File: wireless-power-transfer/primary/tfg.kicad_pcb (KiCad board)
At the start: 2 copper layers, 160 x 100 mm, 35 parts, among them J1 CONN_01X06, J2 Screw_Terminal_1x02, J3 BARREL_JACK, Q1 IRLB8721PBF, Q2 IRLB8721PBF, Q3 IRLB8721PBF, Q4 IRLB8721PBF, U1 PIC18F45K20-I/PT, U2 IR2110, U3 IR2110, U4 R-78E15, U5 R-78E3.3, U6 XBEE_Wi-Fi

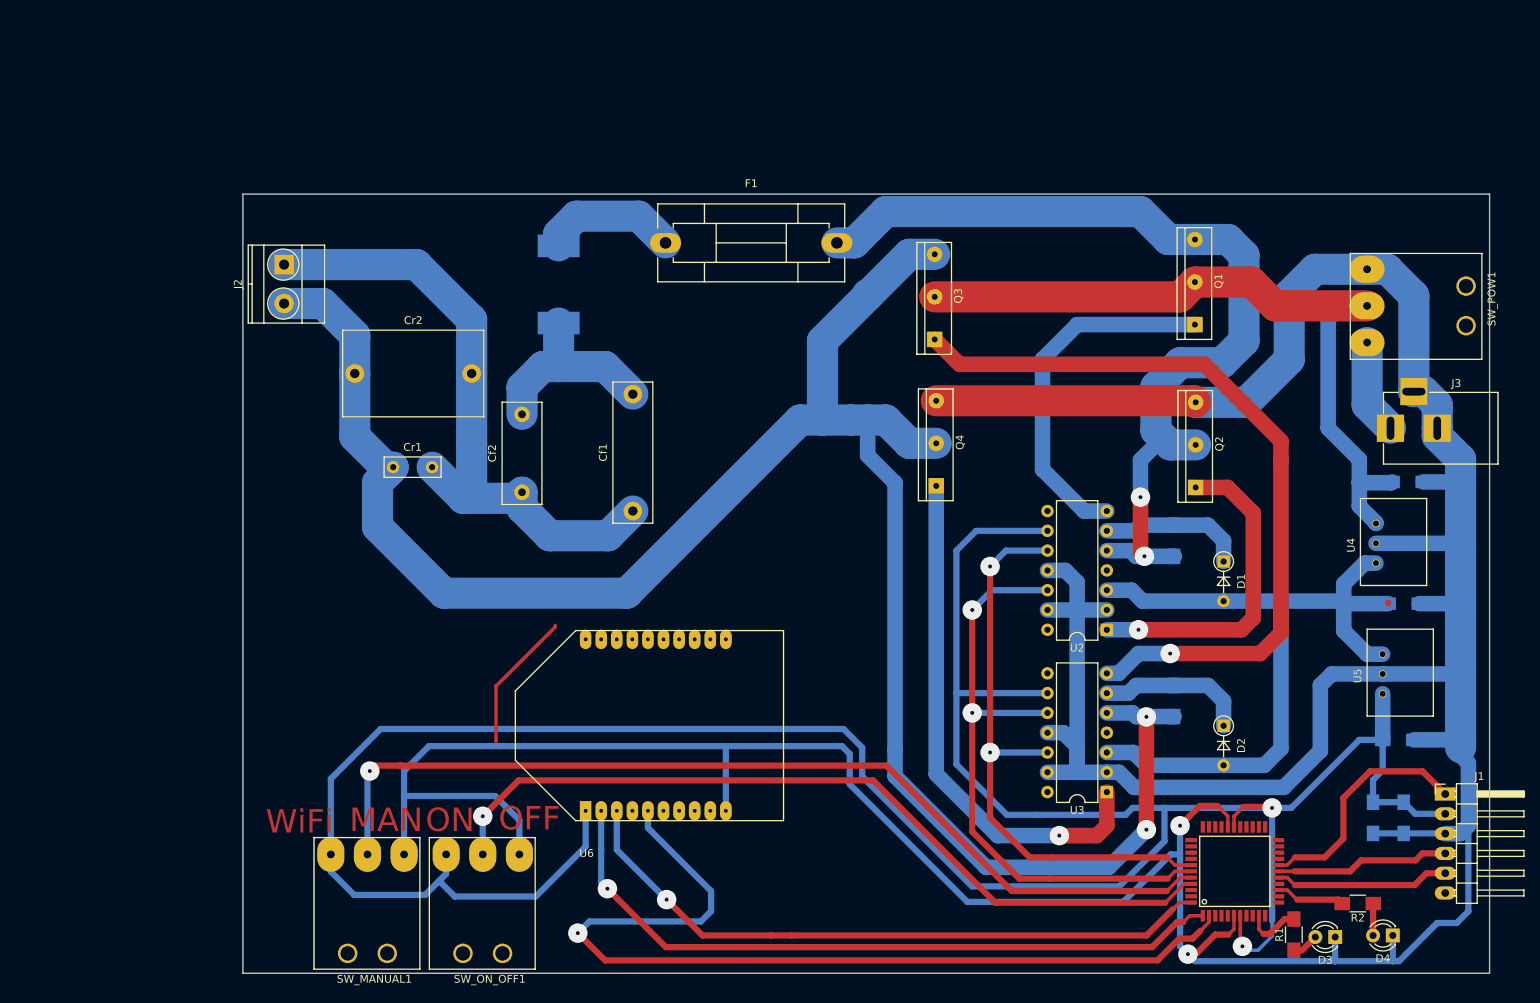
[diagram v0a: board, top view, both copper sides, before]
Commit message: Modified traces for giving some margin to the edges of the board.
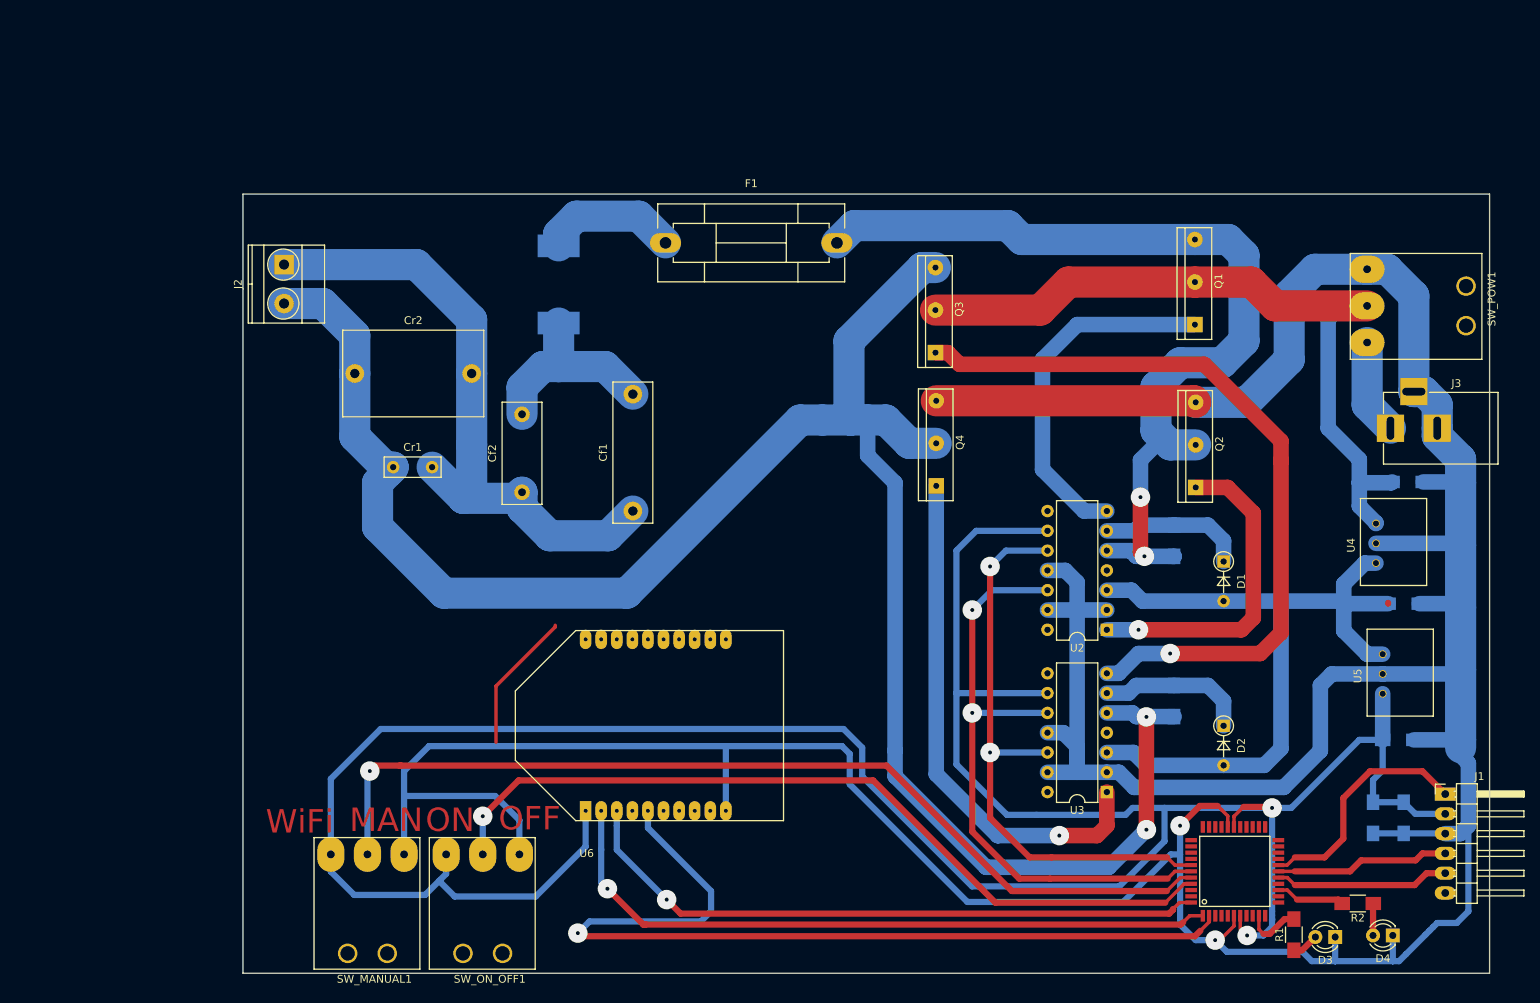
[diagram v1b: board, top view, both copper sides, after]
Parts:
- moved Q3 1.70 mm to (174.6, 67.3)
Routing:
- net Net-(C1-Pad2): track 550.2 -> 543.9 mm
- net Net-(Cboot2-Pad2): track 264.3 -> 260.2 mm
- net /+3.3V: track 355.0 -> 351.7 mm
- net Net-(U1-Pad2): track 119.8 -> 117.3 mm
- net Net-(U1-Pad44): track 85.0 -> 82.8 mm
- net Net-(U1-Pad1): track 91.5 -> 89.4 mm
- net Net-(Cboot1-Pad2): track 122.2 -> 120.7 mm
- net Net-(Q3-Pad1): track 99.2 -> 98.4 mm
- net Net-(C5-Pad1): track 96.3 -> 96.9 mm

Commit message: PCB modified extracting the filter and the tank to another PCB.
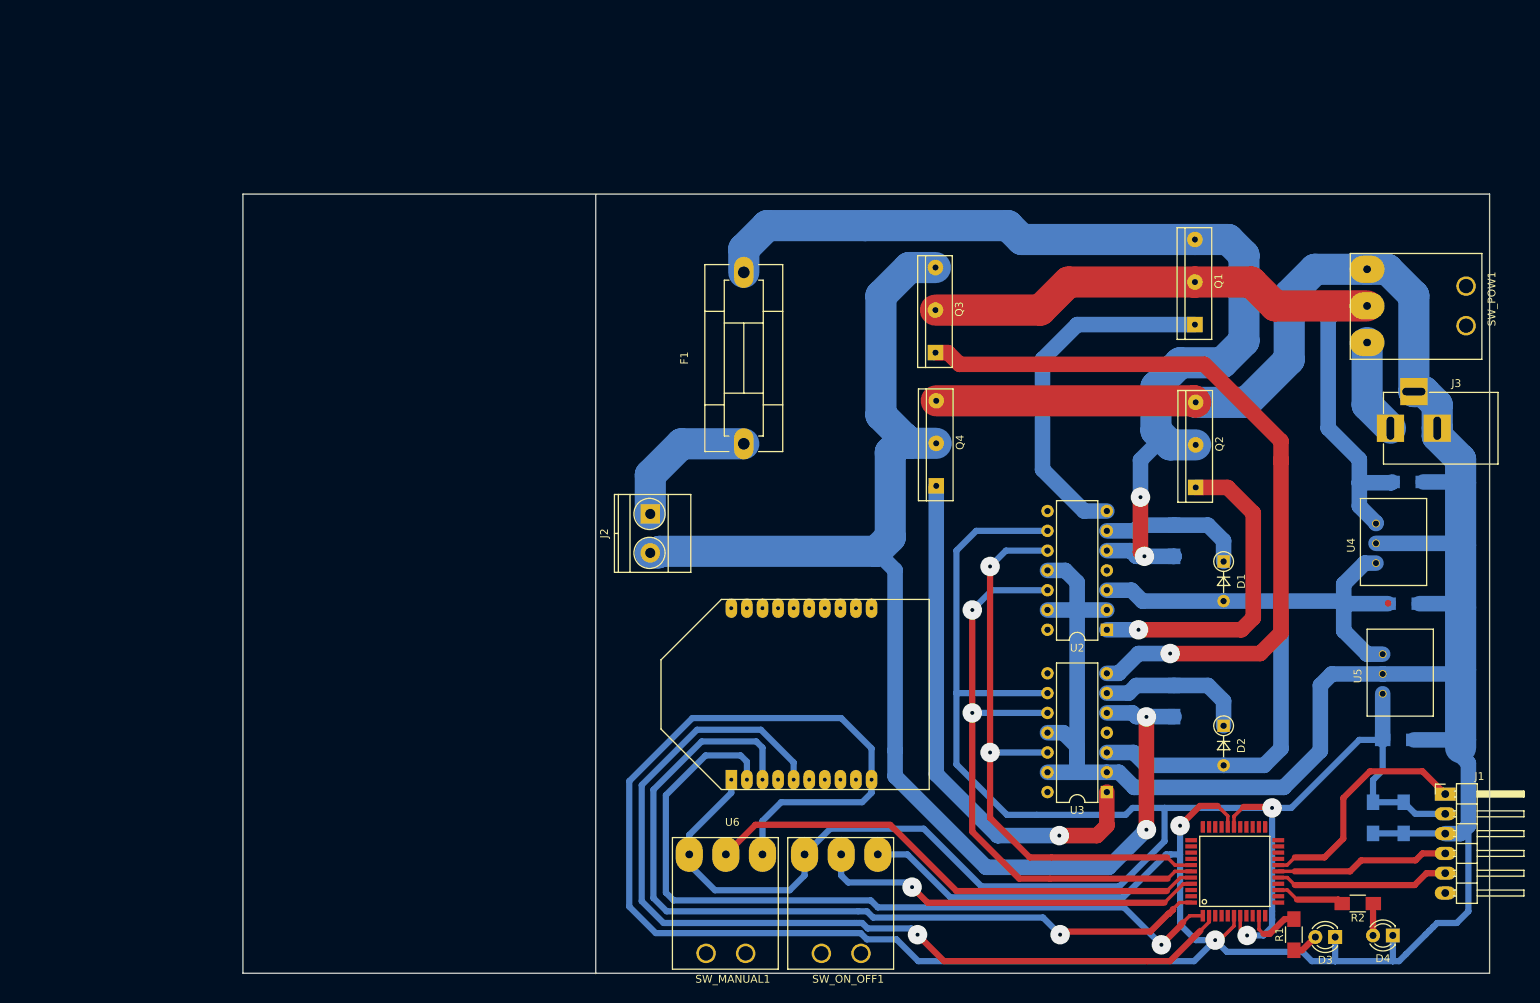
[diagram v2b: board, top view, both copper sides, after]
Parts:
- removed 47uH1: L, Choke_SMD:Choke_SMD_12x12mm_h6mm
- removed Cf1: 47nF, Capacitors_THT:C_Rect_L18.0mm_W5.0mm_P15.00mm_FKS3_FKP3
- removed Cf2: 22nF, Capacitors_THT:C_Rect_L13.0mm_W5.0mm_P10.00mm_FKS3_FKP3_MKS4
- removed Cr1: 150nF, Capacitors_THT:C_Rect_L7.2mm_W2.5mm_P5.00mm_FKS2_FKP2_MKS2_MKP2
- removed Cr2: 470nF, Capacitors_THT:C_Rect_L18.0mm_W11.0mm_P15.00mm_FKS3_FKP3
- moved J2 56.9 mm to (138.0, 88.0)
- moved SW_ON_OFF1 46.0 mm to (157.8, 131.7)
- moved SW_MANUAL1 46.0 mm to (143.0, 131.7)
- moved F1 27.7 mm to (150.0, 79.0), turned to 90 degrees
- moved U6 19.1 mm to (148.4, 122.1)
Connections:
- F1 pad 1: Net-(47uH1-Pad1) -> Net-(F1-Pad1)
- J2 pad 1: Net-(Cf1-Pad1) -> Net-(F1-Pad1)
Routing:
- net /+3.3V: track 351.7 -> 256.5 mm
- net Net-(Cboot2-Pad2): track 260.2 -> 169.9 mm
- net Net-(Cf1-Pad1): track 82.9 -> 0.00 mm
- net Net-(SW_MANUAL1-Pad2): track 124.5 -> 65.5 mm, vias 1 -> 0
- net Net-(SW_ON_OFF1-Pad2): track 105.2 -> 50.1 mm
- net Net-(C1-Pad2): track 543.9 -> 590.2 mm
- net Net-(47uH1-Pad2): track 26.9 -> 0.00 mm
- net Net-(U1-Pad44): track 82.8 -> 108.1 mm
- net Net-(F1-Pad1): track 0.00 -> 18.7 mm
- net (no net): track 18.2 -> 0.09 mm
- net Net-(47uH1-Pad1): track 17.6 -> 0.00 mm
- net Net-(Cboot1-Pad2): track 120.7 -> 136.0 mm
- net Net-(U1-Pad1): track 89.4 -> 100.9 mm
- net Net-(U1-Pad2): track 117.3 -> 120.2 mm
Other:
- outline, holes or cut-outs redrawn
- board text removed: "MAN"
- board text removed: "OFF"
- board text removed: "ON"
- board text removed: "WiFi"

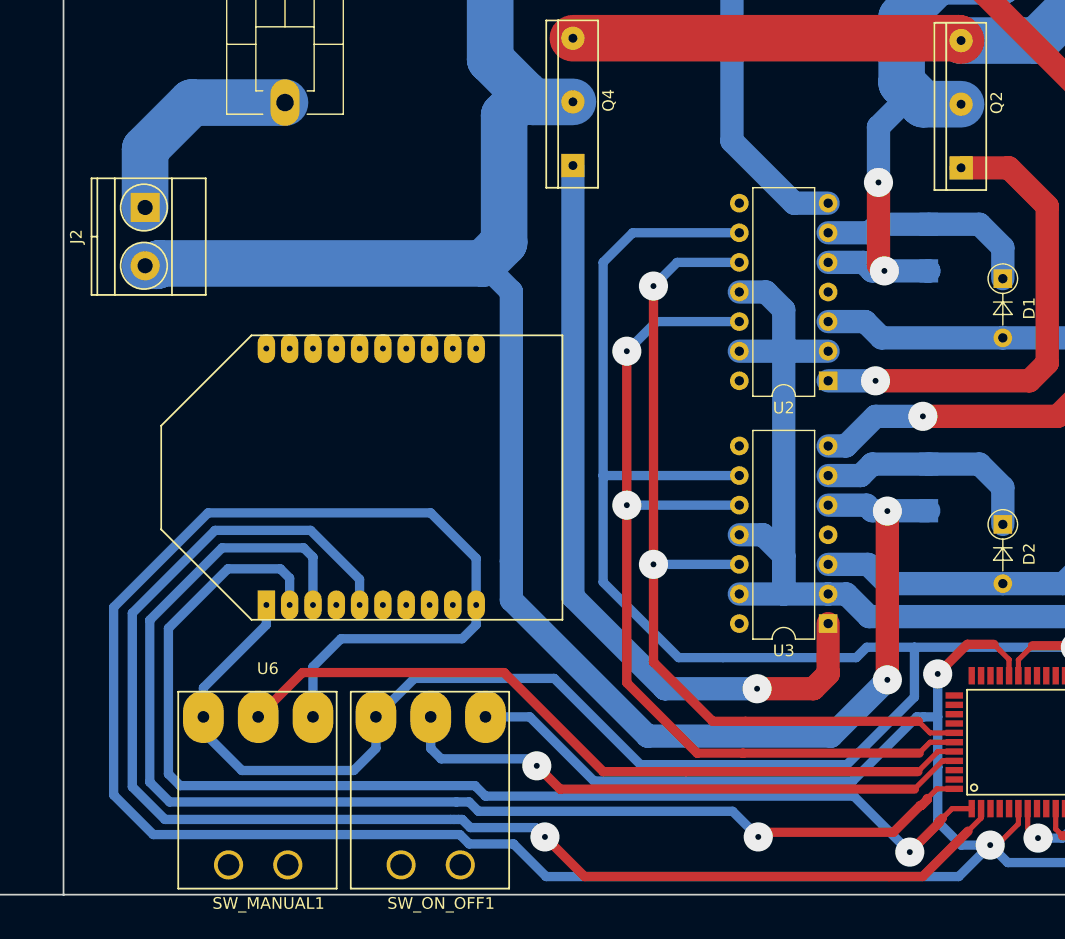
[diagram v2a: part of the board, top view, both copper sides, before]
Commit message: Added switch labels.
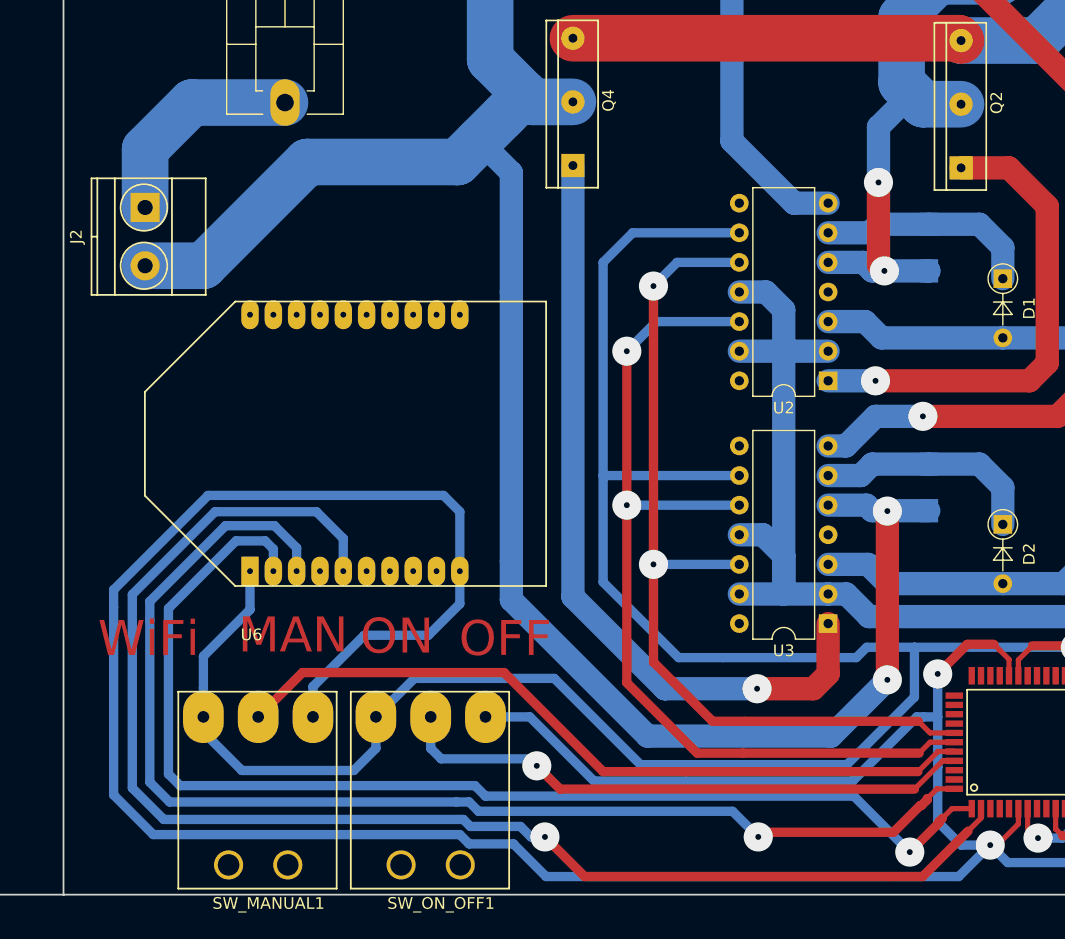
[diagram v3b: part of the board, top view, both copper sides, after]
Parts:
- moved U6 3.22 mm to (147.0, 119.2)
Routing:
- net Net-(Cboot2-Pad2): track 169.9 -> 174.2 mm
- net /+3.3V: track 256.5 -> 258.8 mm
- net Net-(U1-Pad44): track 108.1 -> 106.7 mm
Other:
- board text added: "MAN"
- board text added: "OFF"
- board text added: "ON"
- board text added: "WiFi"
